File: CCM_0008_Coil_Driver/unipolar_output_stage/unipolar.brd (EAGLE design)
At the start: 177.8 x 101.6 mm, 209 parts, among them IC1 AD8675, IC10 AD8675, IC11 AD825, IC12 AD825, IC13 AD825, IC14 AD825, IC15 AD825, IC16 AD825, IC17 BUF634U, IC2 AD797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

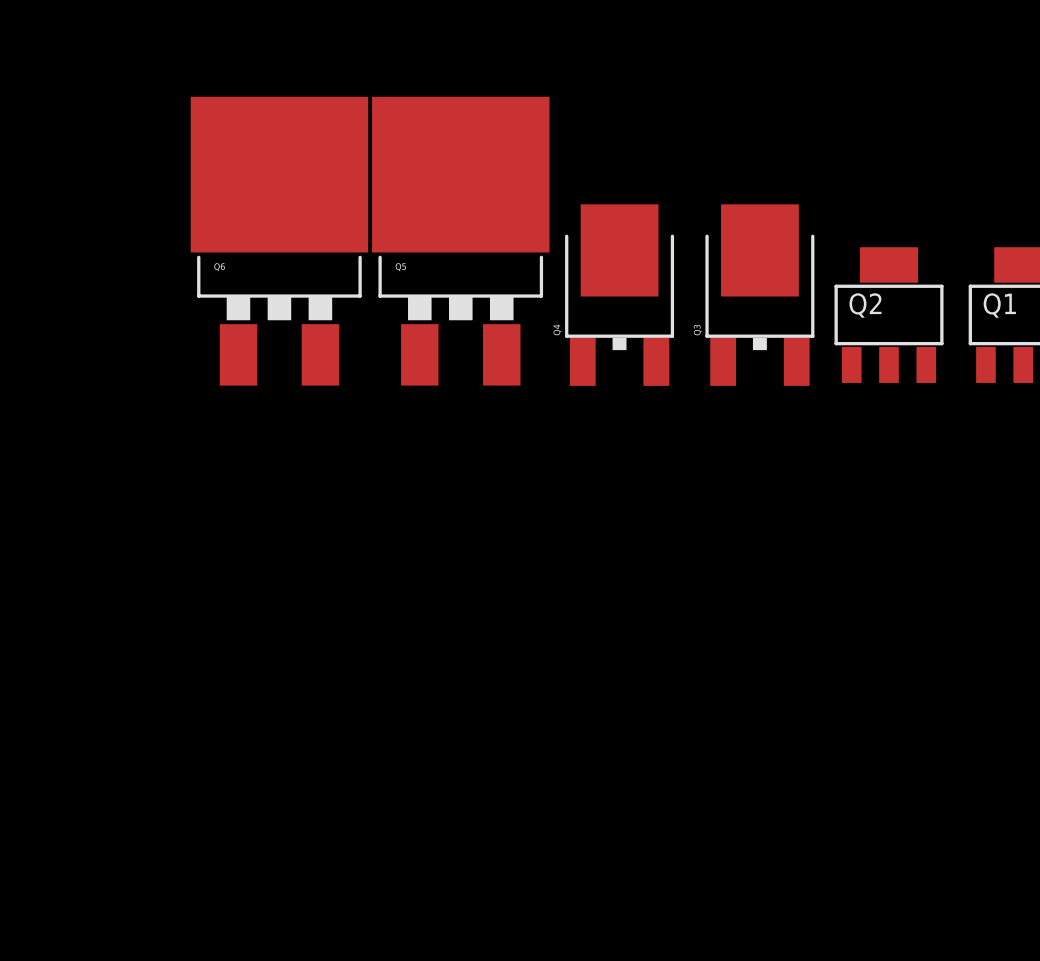
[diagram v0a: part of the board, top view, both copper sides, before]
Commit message: CCM_0008: added preliminary output stage design
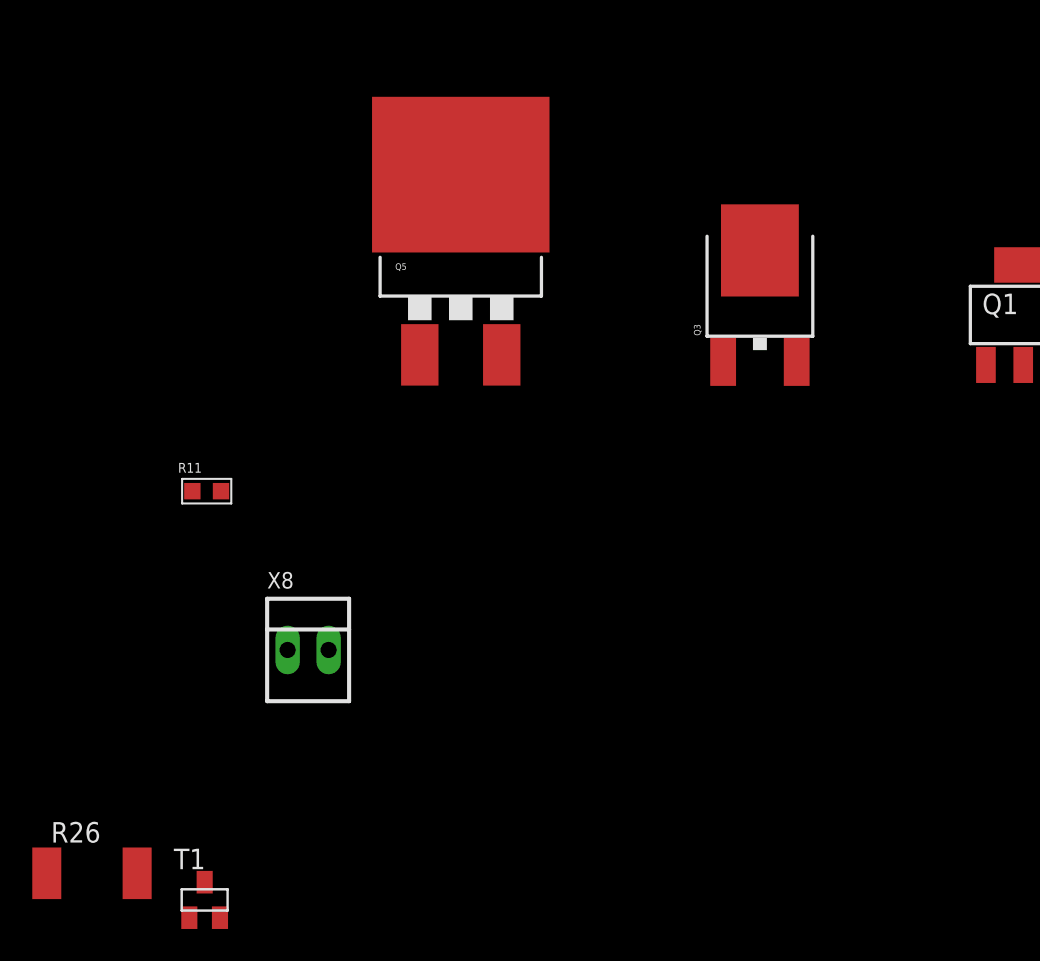
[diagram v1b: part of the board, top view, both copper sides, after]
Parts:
- removed Q2: N-HEXFET_SOT323-, transistor-power:SOT223
- removed Q4: (no value), WCSMain:DPAK
- removed Q6: 100A/100V, WCSMain:TO-263/D2PAK
- added R11: 51.1, acrooptics:0603
- added R26: 0, noah:2512
- added T1: 3904SM, noah:SOT23
- added X8: 22-23-2021, con-molex:22-23-2021
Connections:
- new net AGND: R26.1, T1.2
- new net N$10: Q1.3, Q3.3, Q5.3, R26.2, T1.1, X8.2
- new net N$6: Q1.1, Q3.1, Q5.1, R11.1, T1.3, X8.1
